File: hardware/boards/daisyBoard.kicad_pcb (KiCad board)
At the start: 4 copper layers, 100 x 100 mm, 118 parts, among them IC1 TL072HIDR, IC2 TL072HIDR, IC3 TL072HIDR, IC4 TL072HIDR, J1 LEFT Pin ROW, J13 LEFT Pin ROW Daisy, J14 RIGHT Pin ROW DAISY, J15 Daisy Pin Breakout LEFT, J16 Daisy PIN Breakout RIGHT, J2 RIGHT Pin Row, J3 ESP32 Pin Breakout RIGHT, J4 ESP32 Pin Breakout LEFT, U1 MCP6002-xSN, U2 MCP6002-xSN, U3 MCP6002-xSN

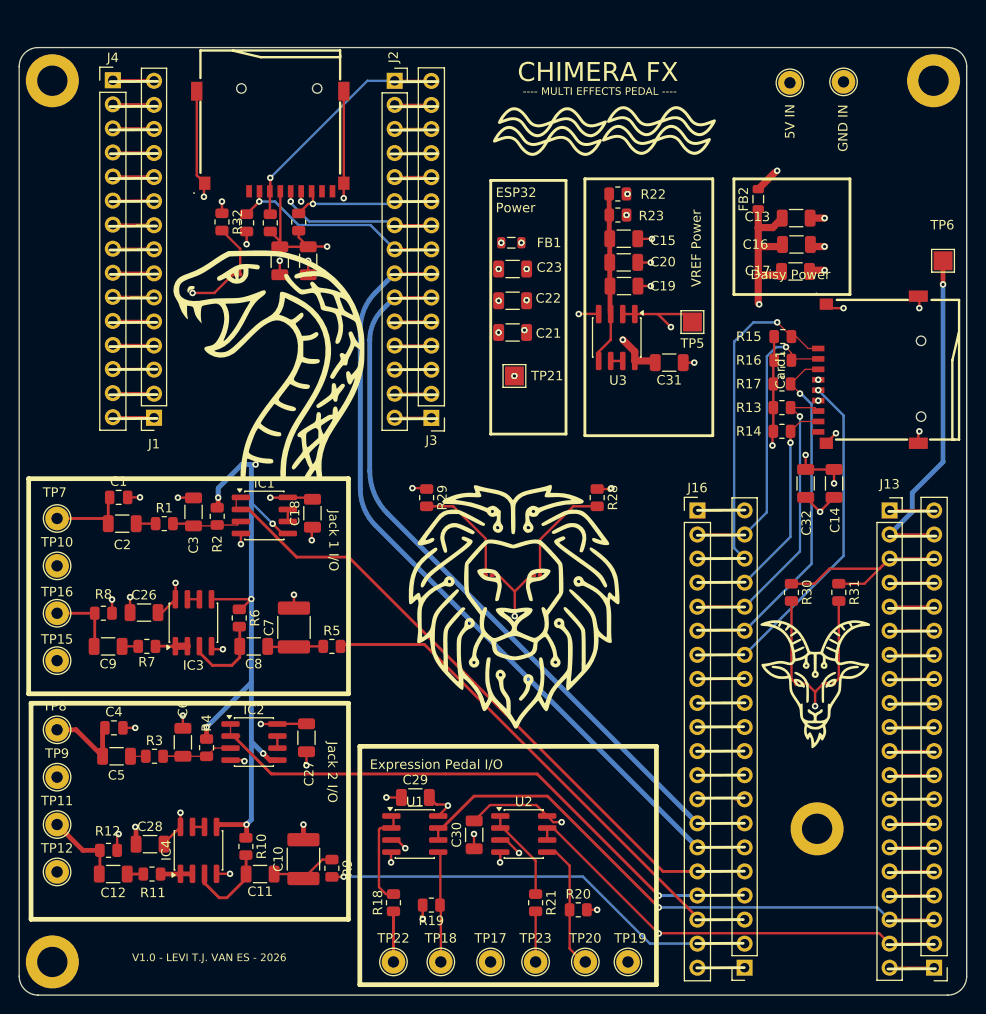
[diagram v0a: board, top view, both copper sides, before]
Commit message: updated some still in pad connections
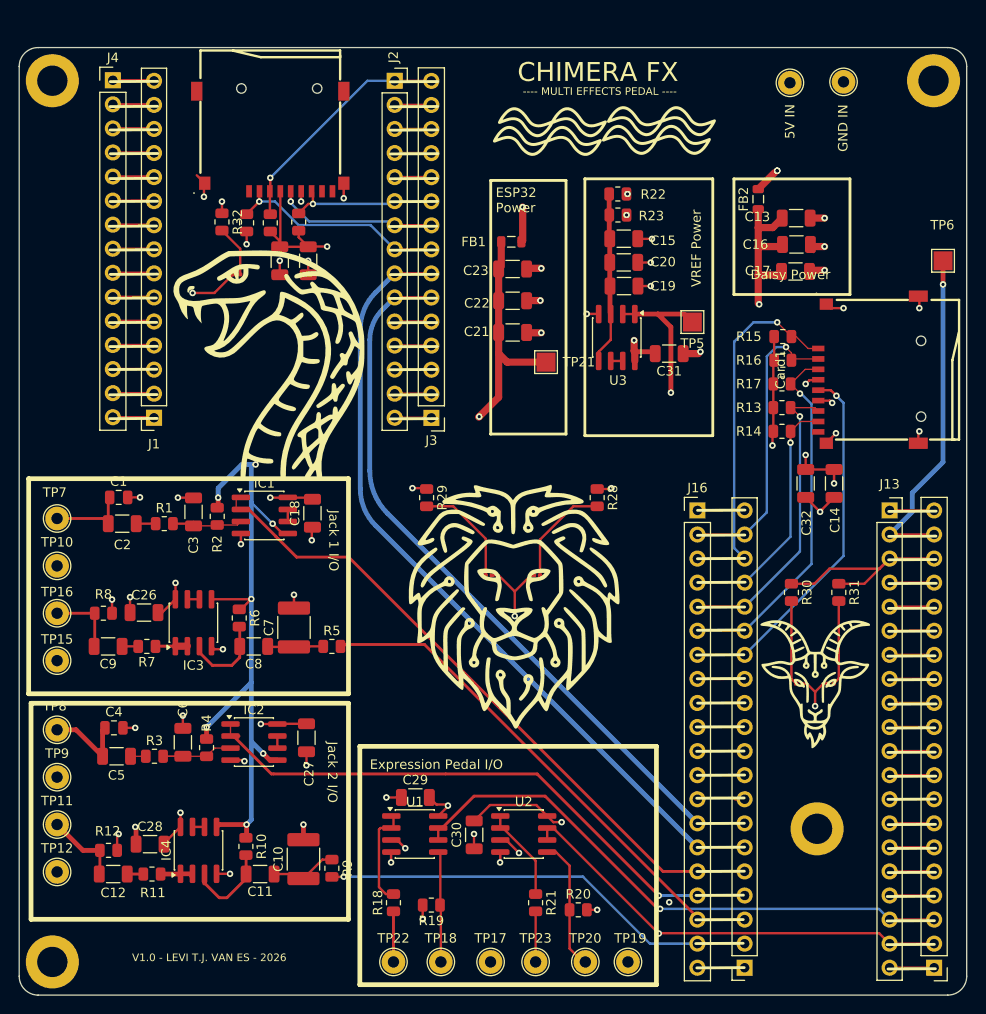
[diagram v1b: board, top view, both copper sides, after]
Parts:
- moved TP21 3.64 mm to (105.6, 83.2)
- moved C31 0.95 mm to (118.6, 82.3)
- moved FB1 0.10 mm to (101.9, 70.5), turned to 180 degrees
- turned C21 to 0 degrees
- turned C22 to 0 degrees
- turned C23 to 0 degrees
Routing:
- net GND: track 118.4 -> 105.9 mm, vias 48 -> 49
- net +5V: track 103.0 -> 98.9 mm, vias 4 -> 5
- net VREF: track 134.2 -> 136.9 mm
- net VCC_ESP32: track 66.7 -> 67.8 mm, vias 5 -> 1
- net /SD_CLK_DAISY: track 38.4 -> 39.2 mm
- net +3.3VD: track 80.8 -> 81.3 mm

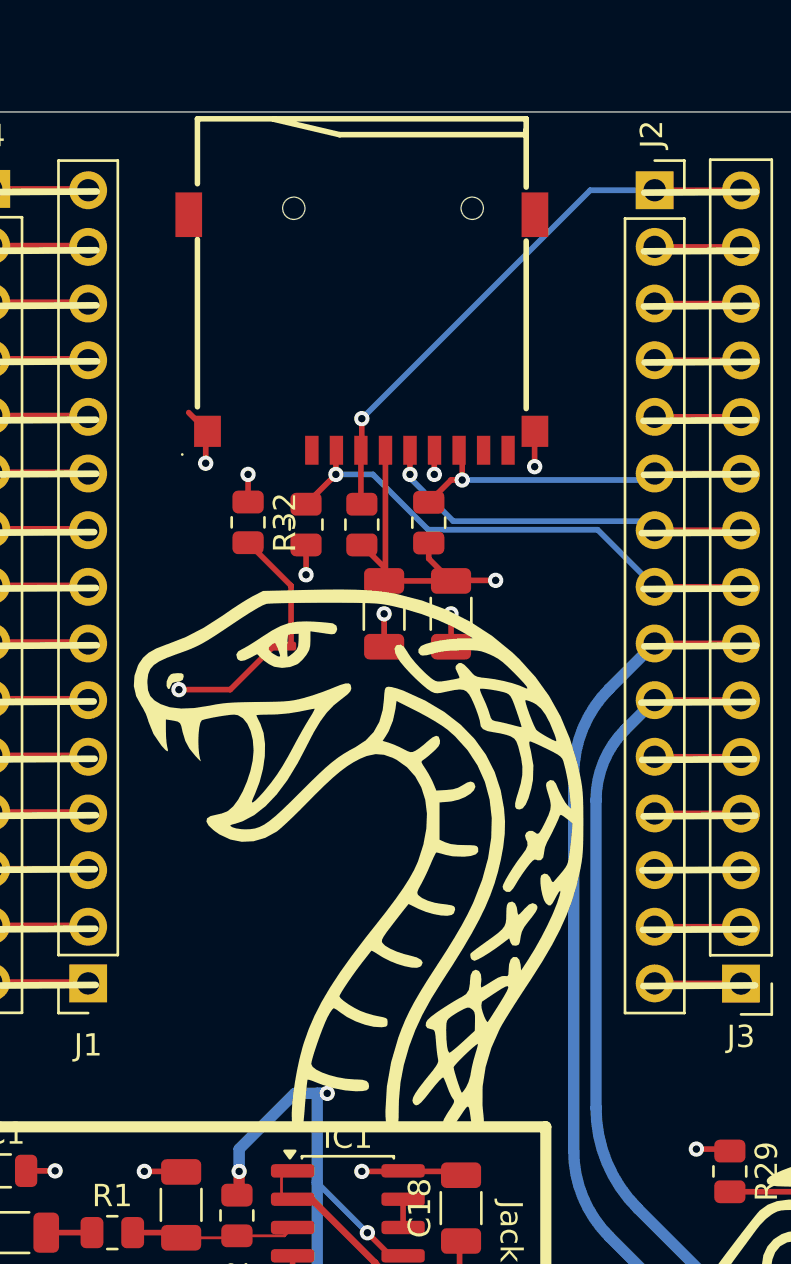
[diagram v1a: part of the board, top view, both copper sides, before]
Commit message: Moved ESP32 SD to keep out of antenna area
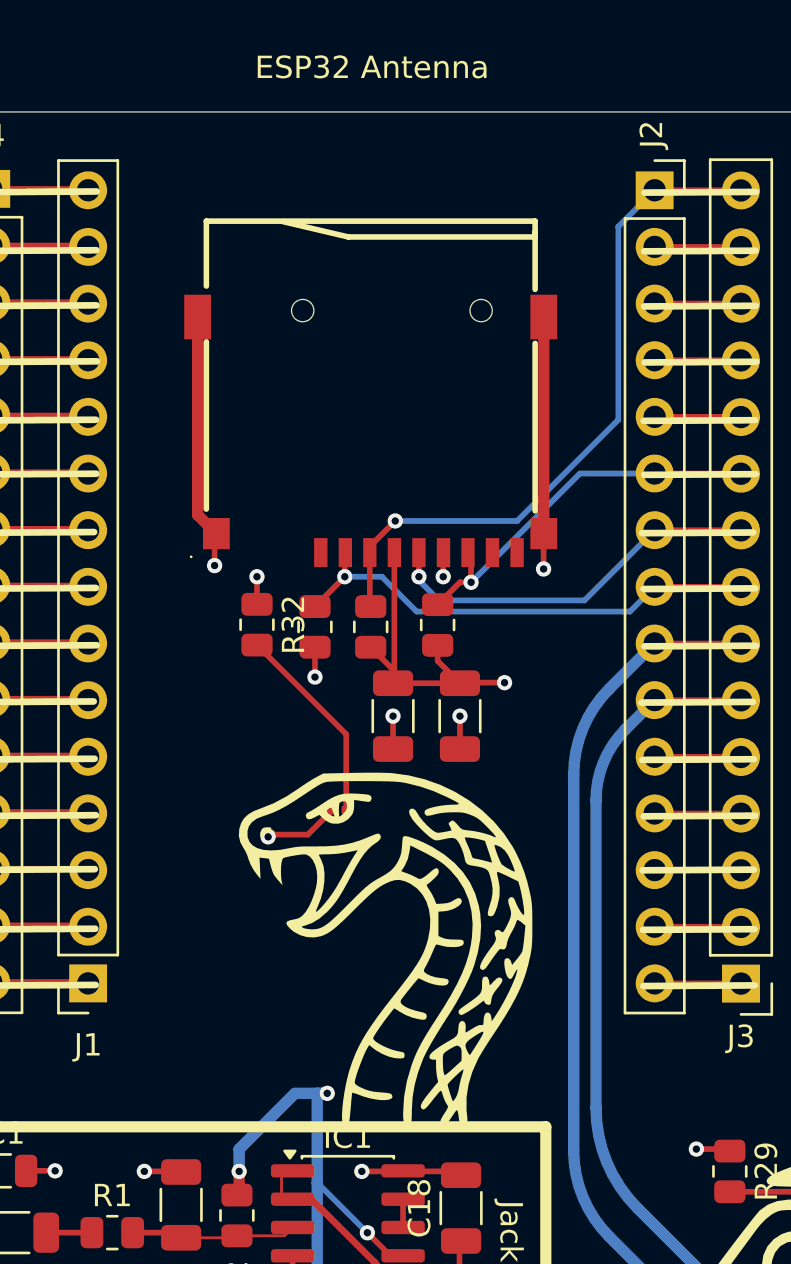
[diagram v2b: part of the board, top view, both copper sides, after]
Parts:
- moved D1 7.76 mm to (75.5, 81.3)
- moved C24 4.60 mm to (77.9, 77.1)
- moved C25 4.60 mm to (80.9, 77.1)
- moved R25 4.60 mm to (79.9, 73.0)
- moved R26 4.60 mm to (74.4, 73.1)
- moved R27 4.60 mm to (76.9, 73.1)
- moved Card2 4.60 mm to (76.9, 64.5)
- moved R32 4.60 mm to (71.8, 73.0)
- moved G*** 4.28 mm to (77.7, 87.3)
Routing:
- net GND: track 105.9 -> 122.7 mm
- net /SD_MOSI: track 25.3 -> 31.2 mm
- net Net-(D1-A): track 5.44 -> 9.07 mm
- net /SD_MISO: track 16.1 -> 18.0 mm
- net /SD_CS: track 24.0 -> 22.6 mm
- net /SD_SCK: track 17.1 -> 17.9 mm
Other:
- board text added: "ESP32 Antenna"

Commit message: last review and update of some things. Still need to adress VREF trace length
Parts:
- added R24: 100, Resistor_SMD:R_0805_2012Metric, F.Cu at (117.7, 80.1)
- moved TP5 13.0 mm to (112.0, 88.3)
- moved C21 4.71 mm to (101.8, 84.8)
- moved C22 4.71 mm to (101.8, 81.4)
- moved FB1 4.71 mm to (101.6, 75.2)
- moved TP21 4.71 mm to (105.3, 87.9)
- moved C23 4.71 mm to (101.8, 78.1)
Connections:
- U3 pad 1: VREF -> Net-(U3A--)
- U3 pad 2: VREF -> Net-(U3A--)
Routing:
- net +5V: track 98.9 -> 103.9 mm, vias 5 -> 4
- net Net-(U3A--): track 0.00 -> 4.12 mm
- net VREF: track 136.9 -> 135.2 mm

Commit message: Changed copper pours to exclude wide area around antenna
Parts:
- U1, U2, U3: value MCP6002-xSN -> MCP6002-I/SN
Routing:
- net GND: vias 49 -> 51

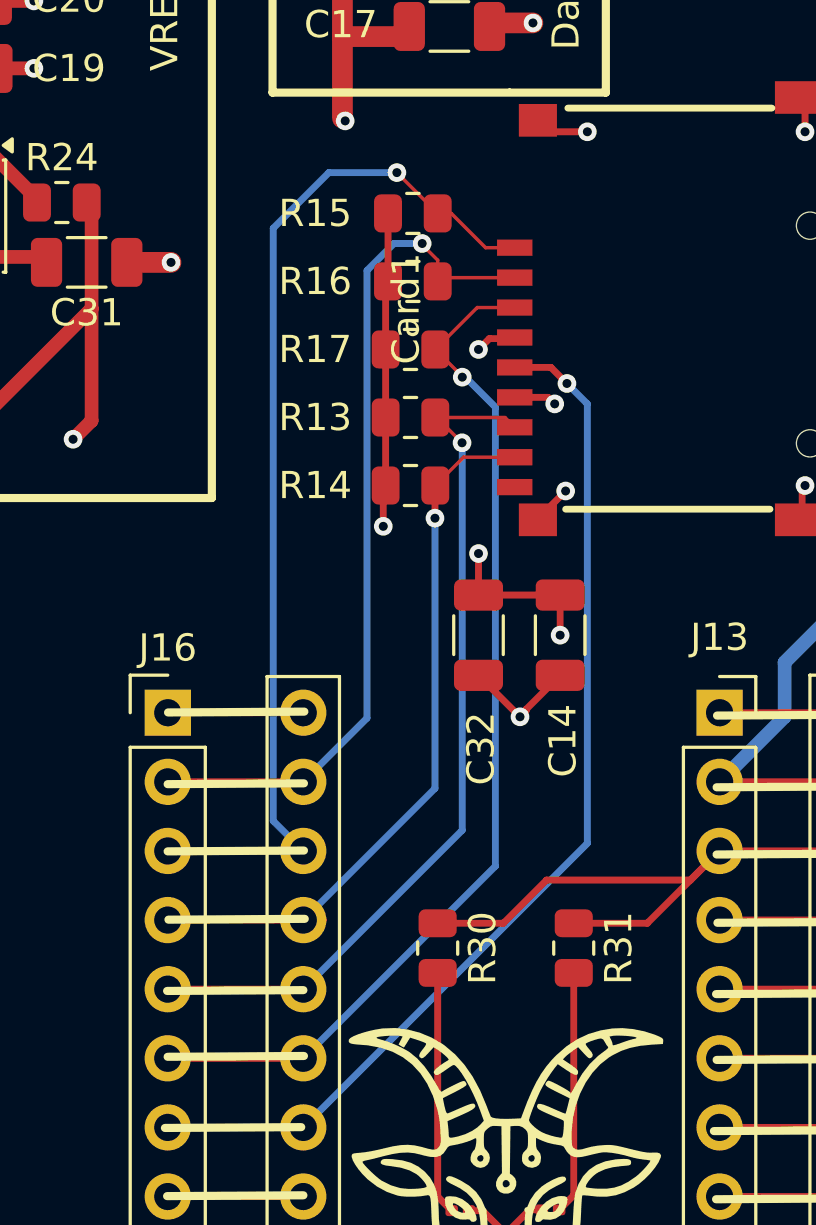
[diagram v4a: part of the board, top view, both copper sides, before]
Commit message: added new review and changed VREF to lower capacitance and lower resistors to reduce load time of the circuit to get to VREF
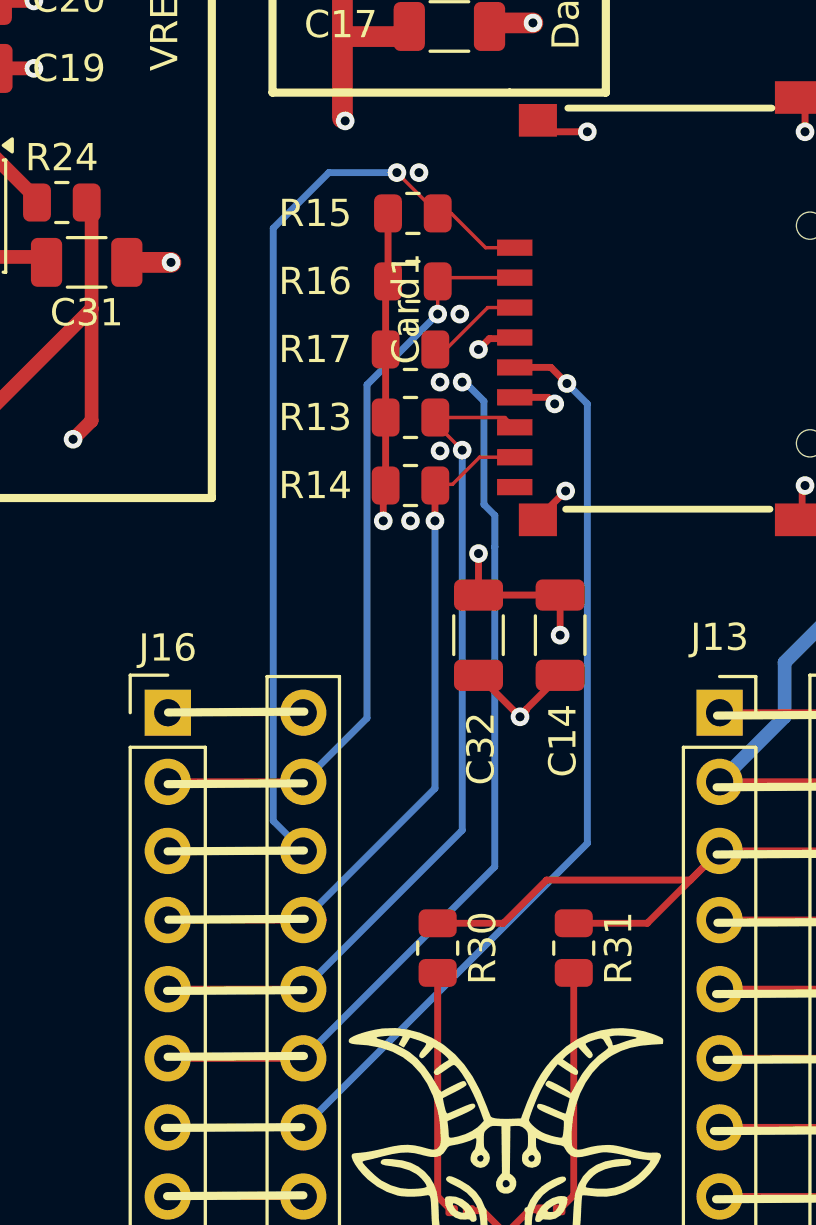
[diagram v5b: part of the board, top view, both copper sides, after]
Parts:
- C15: value 100u -> 10u
- R22, R23: value 100k -> 10k
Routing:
- net /SD_DAT_3_DAISY: track 31.8 -> 28.4 mm
- net /SD_CMD_DAISY: track 38.6 -> 37.1 mm
- net GND: vias 51 -> 56
